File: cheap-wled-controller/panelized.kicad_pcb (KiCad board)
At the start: 2 copper layers, 98 x 96 mm, 94 parts, among them J10 Conn_01x05_Pin, J2 USB_C_Receptacle, J4 Conn_02x05_Odd_Even, J6 Conn_01x05_Pin, J7 Conn_01x02_Pin, J8 Conn_01x07_Pin, SW1 SW_Push, U1 USBLC6-2SC6, U3 CH224K, U4 MX5014S, U5 ESP32-S3-WROOM-1-N4R2, U7 TPS54202DDC, U9 AMS1117-3.3

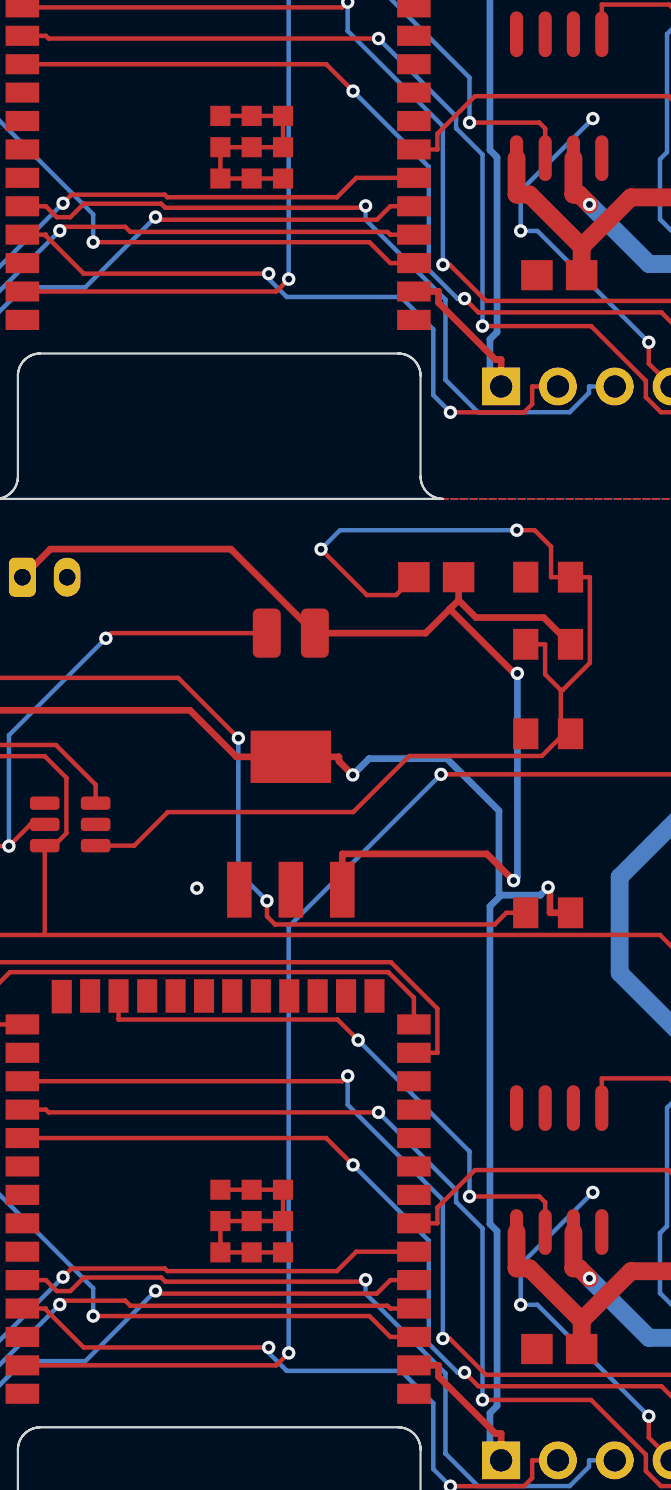
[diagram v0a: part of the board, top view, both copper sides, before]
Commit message: added some GND for the esp32
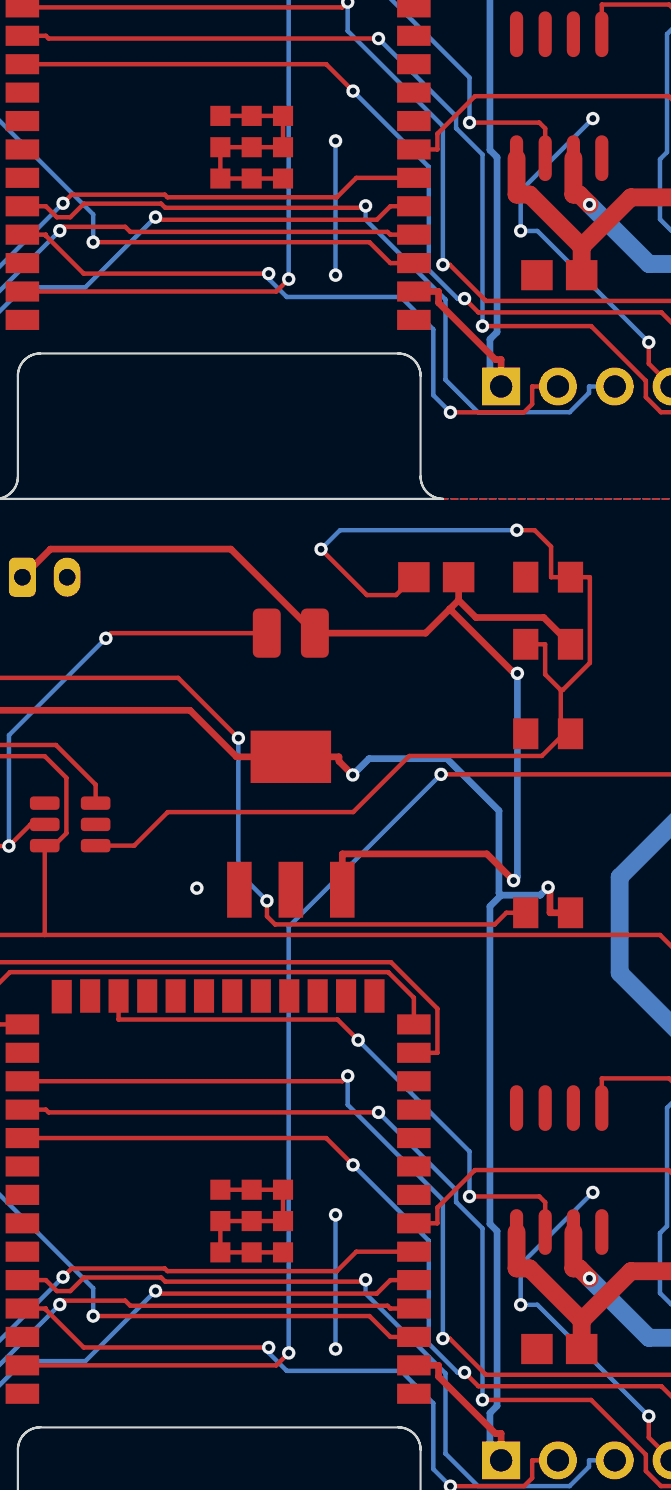
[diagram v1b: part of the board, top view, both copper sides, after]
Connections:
- U5 pad 1: Board_0-unconnected-(U5-GND-Pad1) -> Board_0-GND
- U5 pad 41: Board_0-unconnected-(U5-EPAD-Pad41) -> Board_0-GND
- U5 pad 1: Board_1-unconnected-(U5-GND-Pad1) -> Board_1-GND
- U5 pad 41: Board_1-unconnected-(U5-EPAD-Pad41) -> Board_1-GND
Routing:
- net Board_1-GND: track 19.8 -> 37.0 mm, vias 7 -> 9
- net Board_0-GND: track 19.8 -> 37.0 mm, vias 7 -> 9
- net Board_1-unconnected-(U5-EPAD-Pad41): track 11.2 -> 0.00 mm
- net Board_0-unconnected-(U5-EPAD-Pad41): track 11.2 -> 0.00 mm

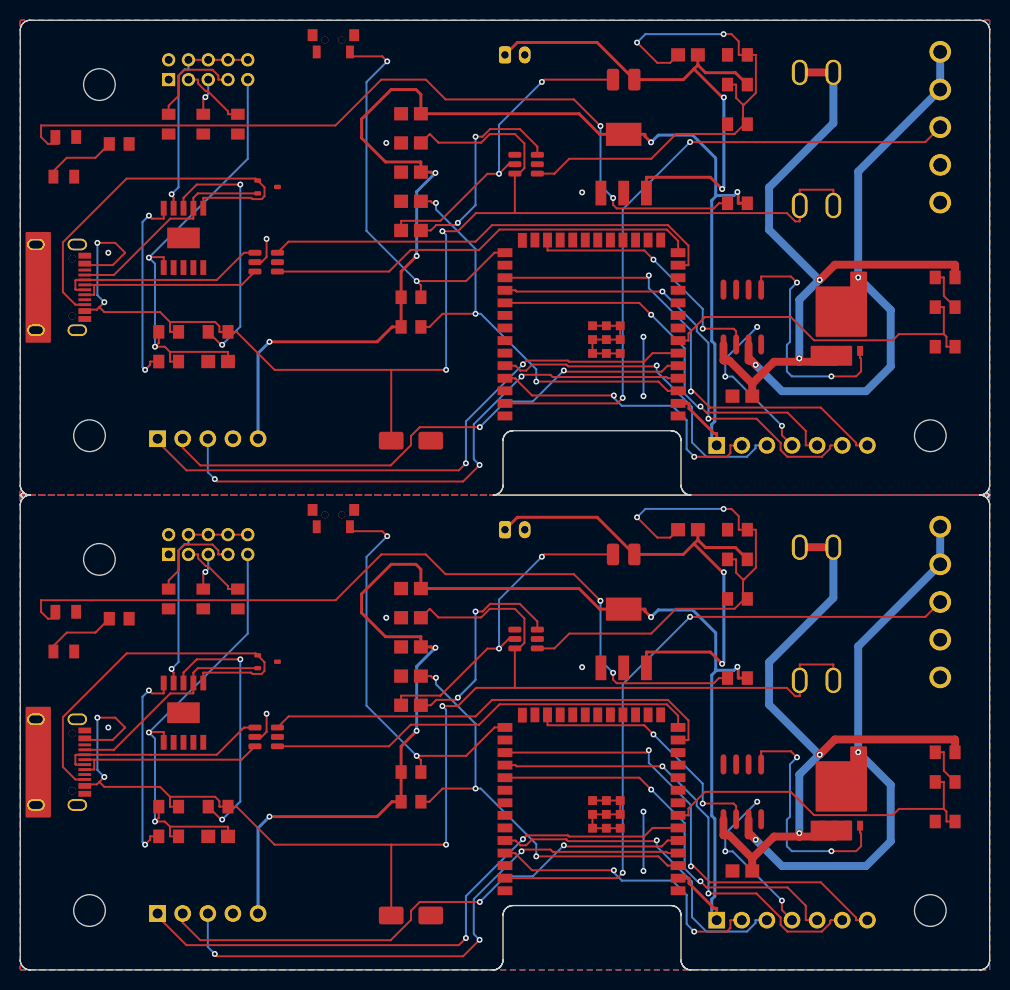
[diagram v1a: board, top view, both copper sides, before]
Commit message: right position for the holes
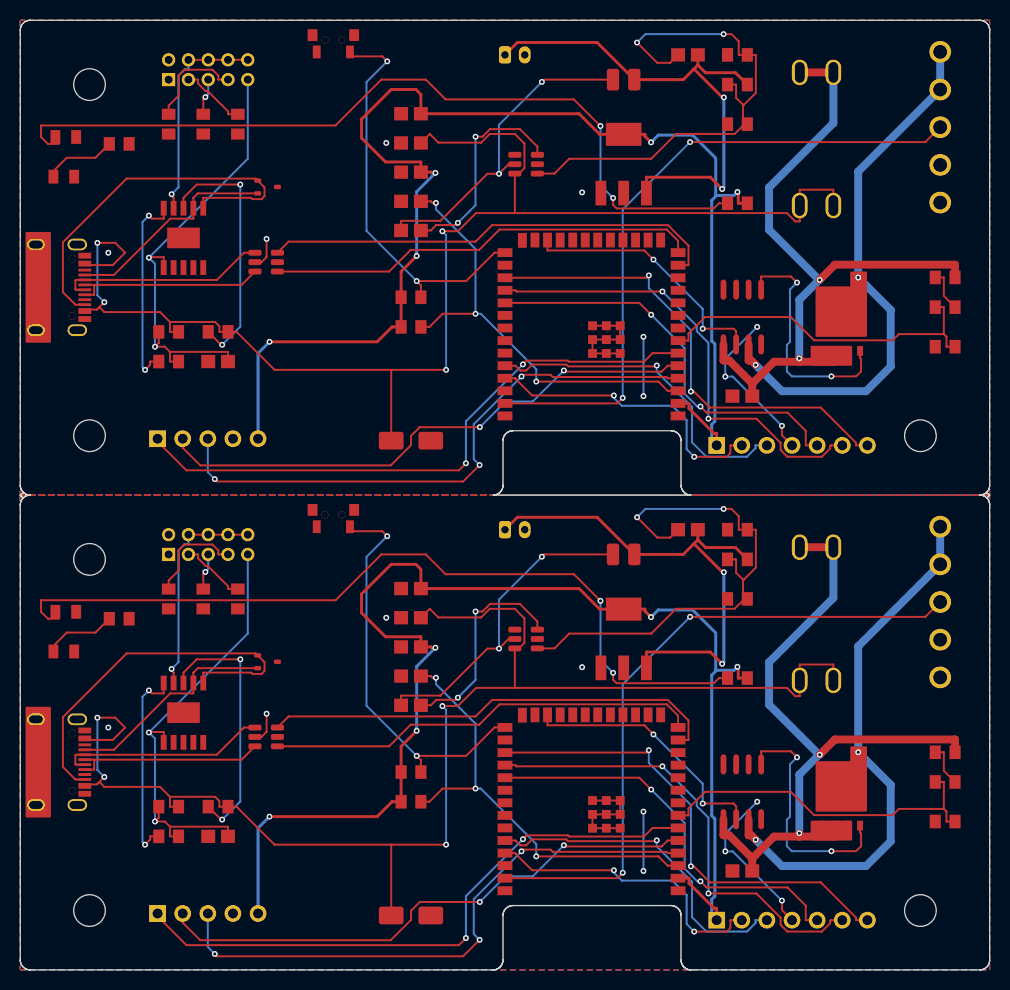
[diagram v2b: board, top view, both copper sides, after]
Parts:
- removed the H1 at (107.5, 26.5)
- removed the H1 at (107.5, 74.5)
- removed the H3 at (191.5, 62.0)
- removed the H3 at (191.5, 110.0)
- added H1: ~, MountingHole:MountingHole_3.2mm_M3, F.Cu at (106.5, 74.5)
- added H1: ~, MountingHole:MountingHole_3.2mm_M3, F.Cu at (106.5, 26.5)
- added H3: ~, MountingHole:MountingHole_3.2mm_M3, F.Cu at (190.5, 62.0)
- added H3: ~, MountingHole:MountingHole_3.2mm_M3, F.Cu at (190.5, 110.0)
